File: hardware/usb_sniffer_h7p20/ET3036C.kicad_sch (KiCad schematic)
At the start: 27 parts, among them U11 EA3036C

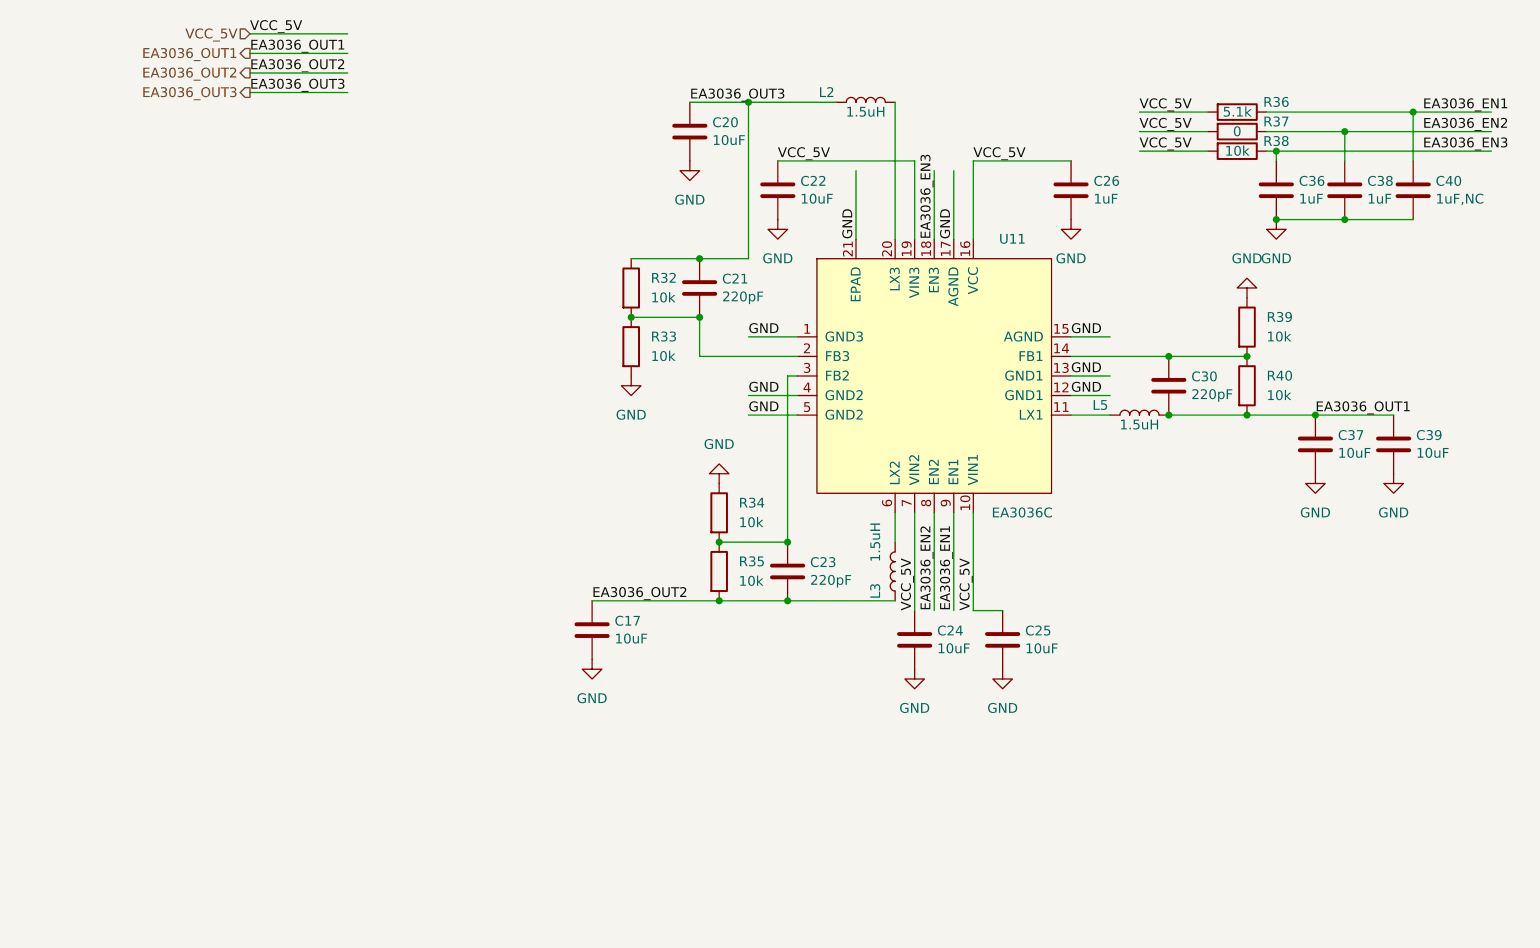
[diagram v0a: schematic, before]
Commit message: 增加辅助电路和优化焊盘工艺
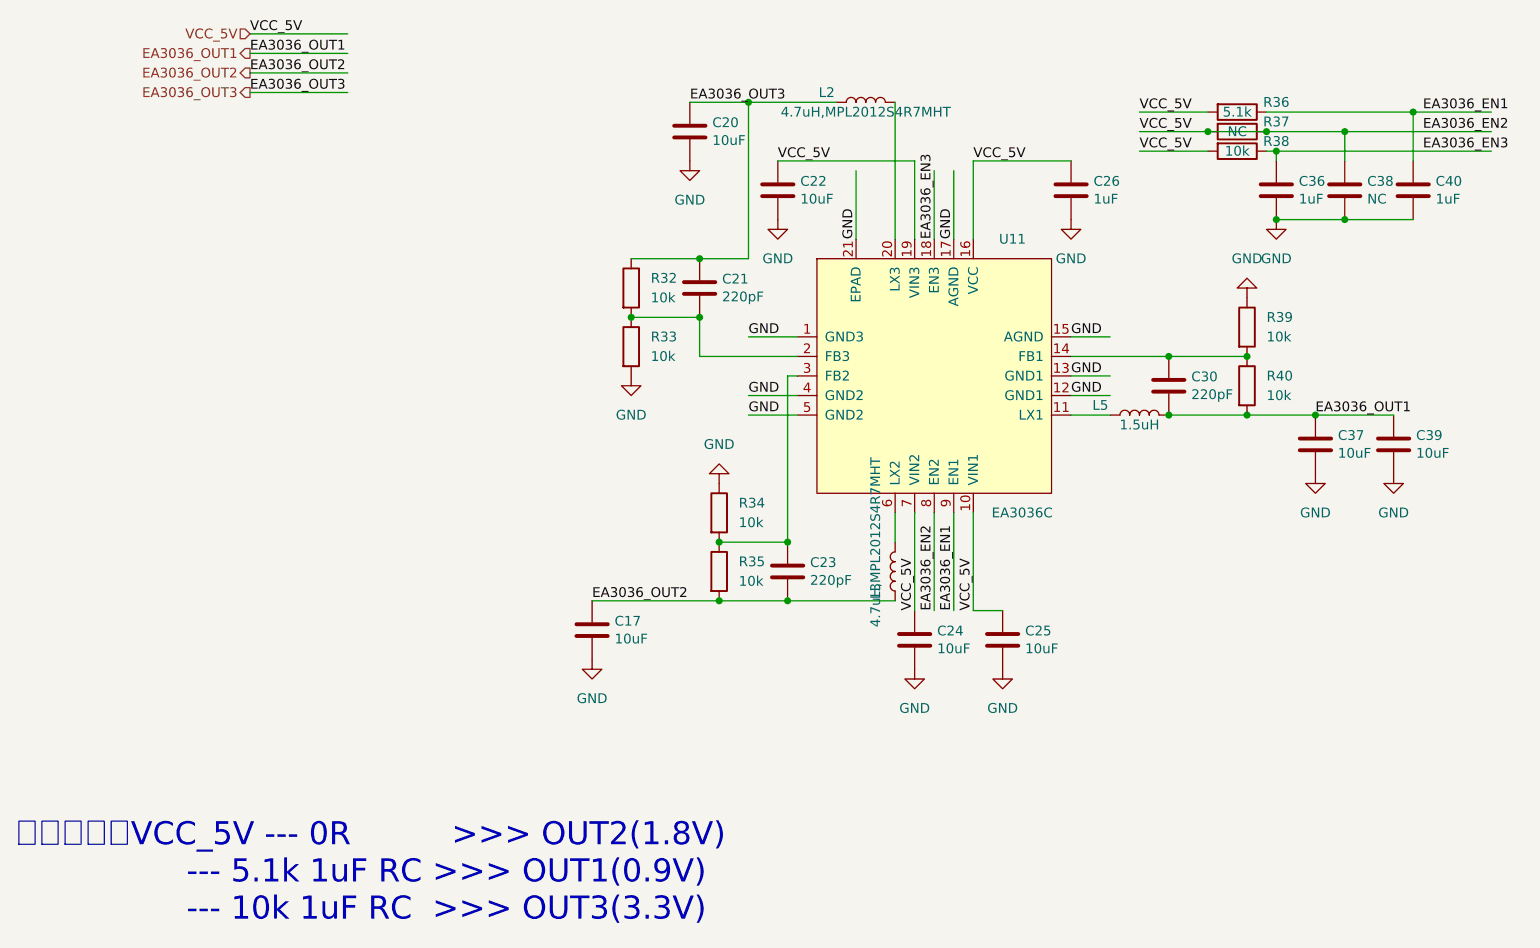
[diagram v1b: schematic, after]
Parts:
- C38: value 1uF -> NC
- C40: value 1uF,NC -> 1uF
- L2, L3: value 1.5uH -> 4.7uH,MPL2012S4R7MHT
- R37: value 0 -> NC
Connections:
- net EA3036_EN2 is gone; now on net VCC_5V: C38.2, R37.1, U11.8 (EN2)
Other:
- note added: "上电顺序：VCC_5V --- 0R >>> OUT2(1.8V) --- 5.1k 1uF RC >>> OUT1(0.9V) --- 10k 1uF RC >>> OUT3(3.3V)"
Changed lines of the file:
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@@
   (junction (at 111.76 81.28) (diameter 0) (color 0 0 0 0)
   )
+  (junction (at 185.42 64.77) (diameter 0) (color 0 0 0 0)
+  )
   (junction (at 111.76 88.9) (diameter 0) (color 0 0 0 0)
   )
@@
   (junction (at 186.69 76.2) (diameter 0) (color 0 0 0 0)
   )
+  (junction (at 177.8 64.77) (diameter 0) (color 0 0 0 0)
+  )
   (junction (at 195.58 64.77) (diameter 0) (color 0 0 0 0)
   )
@@
     (stroke (width 0) (type default))
   )
+  (wire (pts (xy 177.8 64.77) (xy 185.42 64.77))
+    (stroke (width 0) (type default))
+  )
   (wire (pts (xy 121.92 68.58) (xy 139.7 68.58))
     (stroke (width 0) (type default))
@@
   (wire (pts (xy 195.58 64.77) (xy 214.63 64.77))
     (stroke (width 0) (type default))
+  )
+  (text "上电顺序：VCC_5V --- 0R          >>> OUT2(1.8V)\n                 --- 5.1k 1uF RC >>> OUT1(0.9V)\n                 --- 10k 1uF RC  >>> OUT3(3.3V)"
+    (at 22.86 167.64 0)
+    (effects (font (size 3 3)) (justify left bottom))
   )
   (label "EA3036_EN2" (at 205.74 64.77 0) (fields_autoplaced)
@@
       (effects (font (size 1.27 1.27)) (justify right))
     )
-    (property "Value" "1uF" (at 198.501 73.533 0)
+    (property "Value" "NC" (at 198.501 73.533 0)
       (effects (font (size 1.27 1.27)) (justify right))
     )
@@
       (effects (font (size 1.27 1.27)))
     )
-    (property "Value" "1.5uH" (at 133.35 62.23 90)
+    (property "Value" "4.7uH,MPL2012S4R7MHT" (at 133.35 62.23 90)
       (effects (font (size 1.27 1.27)))
     )
@@
       (effects (font (size 1.27 1.27)))
     )
-    (property "Value" "1.5uH" (at 134.62 118.11 90)
+    (property "Value" "4.7uH,MPL2012S4R7MHT" (at 134.62 118.11 90)
       (effects (font (size 1.27 1.27)))
     )
@@
       (effects (font (size 1.27 1.27)) (justify right))
     )
-    (property "Value" "1uF,NC" (at 207.391 73.533 0)
+    (property "Value" "1uF" (at 207.391 73.533 0)
       (effects (font (size 1.27 1.27)) (justify right))
     )
@@
       (effects (font (size 1.27 1.27)))
     )
-    (property "Value" "0" (at 181.61 64.77 90)
-      (effects (font (size 1.27 1.27)))
-    )
+    (property "Value" "NC" (at 181.61 64.77 90)
+      (effects (font (size 1.27 1.27)))
+    )

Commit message: hardware\usb_sniffer_h7p20\production_files.2025605
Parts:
- R32: value 10k -> 150k,1%
- R33, R39: value 10k -> 33k,1%
- R34, R38: value 10k -> 10k,1%
- R35, R40: value 10k -> 20k,1%
- R36: value 5.1k -> 5.1k,1%
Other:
- note removed: "上电顺序：VCC_5V --- 0R >>> OUT2(1.8V) --- 5.1k 1uF RC >>> OUT1(0.9V) --- 10k 1uF RC >>> OUT3(3.3V)"
- moved on the sheet: R32, R33
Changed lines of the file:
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@@
   (junction (at 114.3 125.73) (diameter 0) (color 0 0 0 0)
   )
-  (junction (at 102.87 88.9) (diameter 0) (color 0 0 0 0)
+  (junction (at 99.06 88.9) (diameter 0) (color 0 0 0 0)
   )
   (junction (at 186.69 67.31) (diameter 0) (color 0 0 0 0)
@@
     (stroke (width 0) (type default))
   )
-  (wire (pts (xy 102.87 88.9) (xy 111.76 88.9))
+  (wire (pts (xy 99.06 88.9) (xy 111.76 88.9))
     (stroke (width 0) (type default))
   )
@@
     (stroke (width 0) (type default))
   )
-  (wire (pts (xy 102.87 81.28) (xy 111.76 81.28))
+  (wire (pts (xy 99.06 81.28) (xy 111.76 81.28))
     (stroke (width 0) (type default))
   )
@@
   (wire (pts (xy 195.58 64.77) (xy 214.63 64.77))
     (stroke (width 0) (type default))
-  )
-  (text "上电顺序：VCC_5V --- 0R          >>> OUT2(1.8V)\n                 --- 5.1k 1uF RC >>> OUT1(0.9V)\n                 --- 10k 1uF RC  >>> OUT3(3.3V)"
-    (at 22.86 167.64 0)
-    (effects (font (size 3 3)) (justify left bottom))
   )
   (label "EA3036_EN2" (at 205.74 64.77 0) (fields_autoplaced)
@@
       (effects (font (size 1.27 1.27)))
     )
-    (property "Value" "10k" (at 181.61 67.31 90)
+    (property "Value" "10k,1%" (at 181.61 67.31 90)
       (effects (font (size 1.27 1.27)))
     )
@@
     )
   )
-  (symbol (lib_id "Device:R") (at 102.87 92.71 0) (unit 1)
-    (in_bom yes) (on_board yes) (dnp no) (fields_autoplaced)
-    (property "Reference" "R33" (at 105.41 91.44 0)
+  (symbol (lib_id "Device:R") (at 99.06 92.71 0) (unit 1)
+    (in_bom yes) (on_board yes) (dnp no) (fields_autoplaced)
+    (property "Reference" "R33" (at 101.6 91.44 0)
       (effects (font (size 1.27 1.27)) (justify left))
     )
-    (property "Value" "10k" (at 105.41 93.98 0)
+    (property "Value" "33k,1%" (at 101.6 93.98 0)
       (effects (font (size 1.27 1.27)) (justify left))
     )
-    (property "Footprint" "Resistor_SMD:R_0402_1005Metric" (at 101.092 92.71 90)
-      (effects (font (size 1.27 1.27)) hide)
-    )
-    (property "Datasheet" "~" (at 102.87 92.71 0)
+    (property "Footprint" "Resistor_SMD:R_0402_1005Metric" (at 97.282 92.71 90)
+      (effects (font (size 1.27 1.27)) hide)
+    )
+    (property "Datasheet" "~" (at 99.06 92.71 0)
       (effects (font (size 1.27 1.27)) hide)
     )
@@
       (effects (font (size 1.27 1.27)) (justify left))
     )
-    (property "Value" "10k" (at 116.84 115.57 0)
+    (property "Value" "10k,1%" (at 116.84 115.57 0)
       (effects (font (size 1.27 1.27)) (justify left))
     )
@@
       (effects (font (size 1.27 1.27)) (justify left))
     )
-    (property "Value" "10k" (at 185.42 91.44 0)
+    (property "Value" "33k,1%" (at 185.42 91.44 0)
       (effects (font (size 1.27 1.27)) (justify left))
     )
@@
       (effects (font (size 1.27 1.27)) (justify left))
     )
-    (property "Value" "10k" (at 116.84 123.19 0)
+    (property "Value" "20k,1%" (at 116.84 123.19 0)
       (effects (font (size 1.27 1.27)) (justify left))
     )
@@
       (effects (font (size 1.27 1.27)))
     )
-    (property "Value" "5.1k" (at 181.61 62.23 90)
+    (property "Value" "5.1k,1%" (at 181.61 62.23 90)
       (effects (font (size 1.27 1.27)))
     )
@@
     )
   )
-  (symbol (lib_id "power:GND") (at 102.87 96.52 0) (unit 1)
-    (in_bom yes) (on_board yes) (dnp no) (fields_autoplaced)
-    (property "Reference" "#PWR032" (at 102.87 102.87 0)
-      (effects (font (size 1.27 1.27)) hide)
-    )
-    (property "Value" "GND" (at 102.87 101.6 0)
-      (effects (font (size 1.27 1.27)))
-    )
-    (property "Footprint" "" (at 102.87 96.52 0)
-      (effects (font (size 1.27 1.27)) hide)
-    )
-    (property "Datasheet" "" (at 102.87 96.52 0)
+  (symbol (lib_id "power:GND") (at 99.06 96.52 0) (unit 1)
+    (in_bom yes) (on_board yes) (dnp no) (fields_autoplaced)
+    (property "Reference" "#PWR032" (at 99.06 102.87 0)
+      (effects (font (size 1.27 1.27)) hide)
+    )
+    (property "Value" "GND" (at 99.06 101.6 0)
+      (effects (font (size 1.27 1.27)))
+    )
+    (property "Footprint" "" (at 99.06 96.52 0)
+      (effects (font (size 1.27 1.27)) hide)
+    )
+    (property "Datasheet" "" (at 99.06 96.52 0)
       (effects (font (size 1.27 1.27)) hide)
     )
@@
       (effects (font (size 1.27 1.27)) (justify left))
     )
-    (property "Value" "10k" (at 185.42 99.06 0)
+    (property "Value" "20k,1%" (at 185.42 99.06 0)
       (effects (font (size 1.27 1.27)) (justify left))
     )
@@
     )
   )
-  (symbol (lib_id "Device:R") (at 102.87 85.09 0) (unit 1)
-    (in_bom yes) (on_board yes) (dnp no) (fields_autoplaced)
-    (property "Reference" "R32" (at 105.41 83.82 0)
+  (symbol (lib_id "Device:R") (at 99.06 85.09 0) (unit 1)
+    (in_bom yes) (on_board yes) (dnp no) (fields_autoplaced)
+    (property "Reference" "R32" (at 101.6 83.82 0)
       (effects (font (size 1.27 1.27)) (justify left))
     )
-    (property "Value" "10k" (at 105.41 86.36 0)
+    (property "Value" "150k,1%" (at 101.6 86.36 0)
       (effects (font (size 1.27 1.27)) (justify left))
     )
-    (property "Footprint" "Resistor_SMD:R_0402_1005Metric" (at 101.092 85.09 90)
-      (effects (font (size 1.27 1.27)) hide)
-    )
-    (property "Datasheet" "~" (at 102.87 85.09 0)
-      (effects (font (size 1.27 1.27)) hide)
-    )
+    (property "Footprint" "Resistor_SMD:R_0402_1005Metric" (at 97.282 85.09 90)
+      (effects (font (size 1.27 1.27)) hide)
+    )
+    (property "Datasheet" "~" (at 99.06 85.09 0)
+      (effects (font (size 1.27 1.27)) hide)
+    )

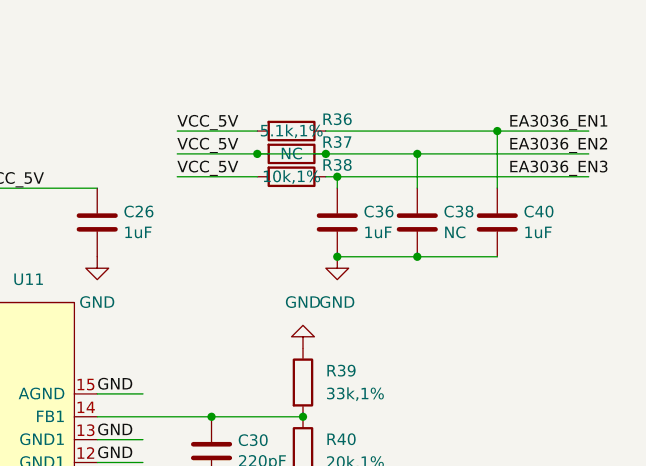
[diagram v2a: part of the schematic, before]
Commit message: 调整上电顺序为 5V -> core 0.95V -> vccaux 1.8V -> vccio
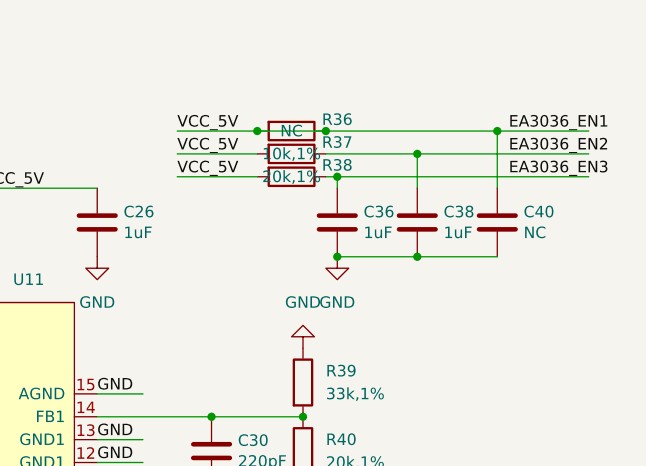
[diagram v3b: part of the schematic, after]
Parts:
- C38: value NC -> 1uF
- C40: value 1uF -> NC
- R36: value 5.1k,1% -> NC
- R37: value NC -> 10k,1%
- R38: value 10k,1% -> 20k,1%
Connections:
- net EA3036_EN1 is gone; now on net VCC_5V: C40.2, R36.1, U11.9 (EN1)
- net VCC_5V: no longer C38.2, R37.1, U11.8 (EN2)
- new net EA3036_EN2: C38.2, R37.1, U11.8 (EN2)
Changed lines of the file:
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@@
   (junction (at 204.47 62.23) (diameter 0) (color 0 0 0 0)
   )
+  (junction (at 185.42 62.23) (diameter 0) (color 0 0 0 0)
+  )
   (junction (at 172.72 93.98) (diameter 0) (color 0 0 0 0)
   )
   (junction (at 111.76 81.28) (diameter 0) (color 0 0 0 0)
   )
-  (junction (at 185.42 64.77) (diameter 0) (color 0 0 0 0)
-  )
   (junction (at 111.76 88.9) (diameter 0) (color 0 0 0 0)
   )
+  (junction (at 177.8 62.23) (diameter 0) (color 0 0 0 0)
+  )
   (junction (at 195.58 76.2) (diameter 0) (color 0 0 0 0)
   )
@@
   (junction (at 186.69 76.2) (diameter 0) (color 0 0 0 0)
   )
-  (junction (at 177.8 64.77) (diameter 0) (color 0 0 0 0)
-  )
   (junction (at 195.58 64.77) (diameter 0) (color 0 0 0 0)
   )
@@
     (stroke (width 0) (type default))
   )
-  (wire (pts (xy 177.8 64.77) (xy 185.42 64.77))
-    (stroke (width 0) (type default))
-  )
   (wire (pts (xy 121.92 68.58) (xy 139.7 68.58))
     (stroke (width 0) (type default))
@@
   )
   (wire (pts (xy 186.69 67.31) (xy 186.69 68.58))
+    (stroke (width 0) (type default))
+  )
+  (wire (pts (xy 177.8 62.23) (xy 185.42 62.23))
     (stroke (width 0) (type default))
   )
@@
       (effects (font (size 1.27 1.27)))
     )
-    (property "Value" "10k,1%" (at 181.61 67.31 90)
+    (property "Value" "20k,1%" (at 181.61 67.31 90)
       (effects (font (size 1.27 1.27)))
     )
@@
       (effects (font (size 1.27 1.27)) (justify right))
     )
-    (property "Value" "NC" (at 198.501 73.533 0)
+    (property "Value" "1uF" (at 198.501 73.533 0)
       (effects (font (size 1.27 1.27)) (justify right))
     )
@@
       (effects (font (size 1.27 1.27)) (justify right))
     )
-    (property "Value" "1uF" (at 207.391 73.533 0)
+    (property "Value" "NC" (at 207.391 73.533 0)
       (effects (font (size 1.27 1.27)) (justify right))
     )
@@
       (effects (font (size 1.27 1.27)))
     )
-    (property "Value" "5.1k,1%" (at 181.61 62.23 90)
+    (property "Value" "NC" (at 181.61 62.23 90)
       (effects (font (size 1.27 1.27)))
     )
@@
       (effects (font (size 1.27 1.27)))
     )
-    (property "Value" "NC" (at 181.61 64.77 90)
-      (effects (font (size 1.27 1.27)))
-    )
+    (property "Value" "10k,1%" (at 181.61 64.77 90)
+      (effects (font (size 1.27 1.27)))
+    )
